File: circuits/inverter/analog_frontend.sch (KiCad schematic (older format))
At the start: 102 parts

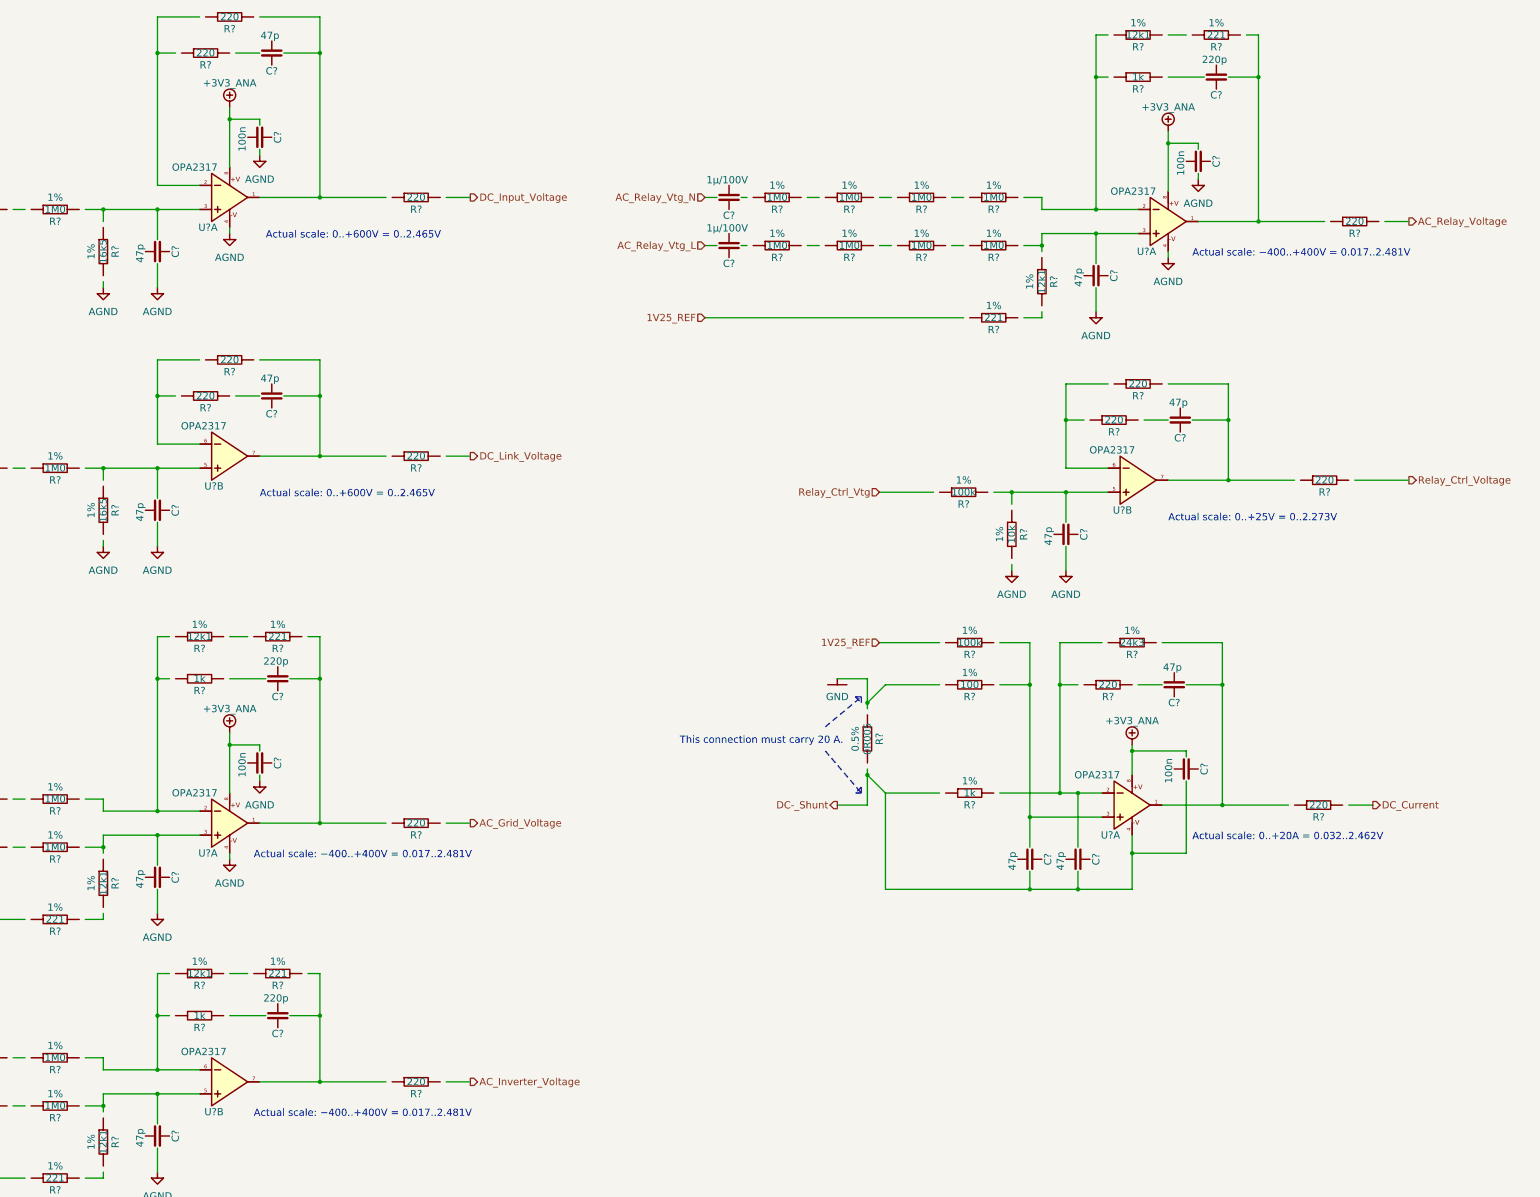
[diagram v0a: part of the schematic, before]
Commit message: Add more circuitry, add library content
AC current measurement
AC filter
AC switch
DC booster
DC input
Analog frontend
drivers
inverter
main controller
power supply

new components for:
standard library (e.g. relay)
AC current sensor acs722
voltage regulator LM317L

Footprints for:
AC relay
TO-220
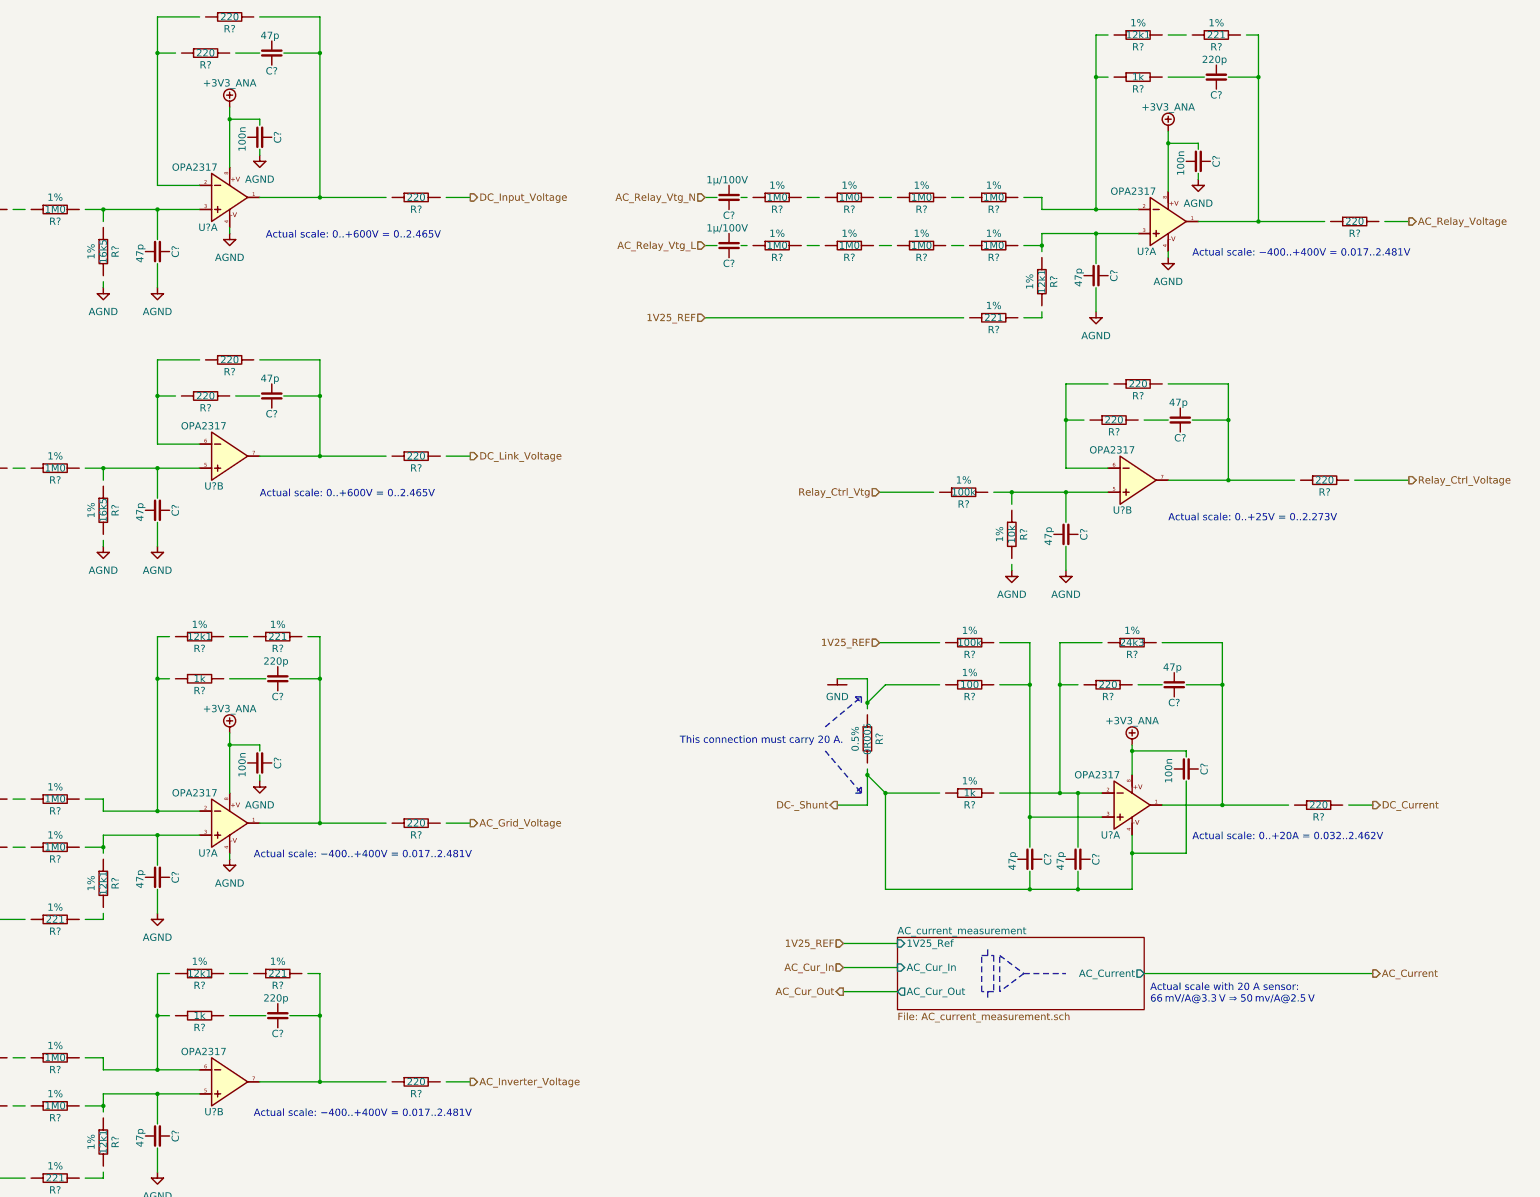
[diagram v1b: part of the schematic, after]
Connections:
- net labels added: AC_Cur_In, AC_Cur_Out, AC_Current
- wire segments 196 -> 249
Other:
- note added: "Actual scale with 20 A sensor:\n66 mV/A@3.3 V ⇒ 50 mv/A@2.5 V"
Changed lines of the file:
@@
 EESchema Schematic File Version 2
+LIBS:lm317
 LIBS:kv30f
 LIBS:OSSI_standard_components
@@
 LIBS:lm4030
 LIBS:power
+LIBS:acs722
 LIBS:OSSI_MK_I-cache
 EELAYER 25 0
@@
 $Descr A3 16535 11693
 encoding utf-8
-Sheet 8 10
+Sheet 8 11
 Title "Analog Frontend"
 Date "2016-03-09"
@@
 	4200 2850 4200 2800
 Wire Wire Line
-	4050 2200 5000 2200
+	4050 2200 4200 2200
+Wire Wire Line
+	4200 2200 4650 2200
+Wire Wire Line
+	4650 2200 5000 2200
 Wire Wire Line
 	4200 2300 4200 2200
@@
 $EndComp
 Wire Wire Line
-	5250 1350 5250 1850
+	5250 1350 5250 1450
+Wire Wire Line
+	5250 1450 5250 1850
 $Comp
 L Capacitor C?
@@
 Connection ~ 5250 1450
 Wire Wire Line
-	5500 2100 6550 2100
+	5500 2100 6000 2100
+Wire Wire Line
+	6000 2100 6550 2100
 $Comp
 L Capacitor C?
@@
 	4650 2000 5000 2000
 Wire Wire Line
-	4650 600  4650 2000
+	4650 600  4650 900
+Wire Wire Line
+	4650 900  4650 2000
 Wire Wire Line
 	4650 600  5000 600
@@
 	5500 600  6000 600
 Wire Wire Line
-	6000 600  6000 2100
+	6000 600  6000 900
+Wire Wire Line
+	6000 900  6000 2100
 Connection ~ 6000 2100
 Wire Wire Line
@@
 	4200 5000 4200 4950
 Wire Wire Line
-	4050 4350 5000 4350
+	4050 4350 4200 4350
+Wire Wire Line
+	4200 4350 4650 4350
+Wire Wire Line
+	4650 4350 5000 4350
 Wire Wire Line
 	4200 4450 4200 4350
@@
 	1400 4350 1750 4350
 Wire Wire Line
-	5500 4250 6550 4250
+	5500 4250 6000 4250
+Wire Wire Line
+	6000 4250 6550 4250
 $Comp
 L Capacitor C?
@@
 	4650 4150 5000 4150
 Wire Wire Line
-	4650 3450 4650 4150
+	4650 3450 4650 3750
+Wire Wire Line
+	4650 3750 4650 4150
 Wire Wire Line
 	4650 3450 5000 3450
@@
 	5500 3450 6000 3450
 Wire Wire Line
-	6000 3450 6000 4250
+	6000 3450 6000 3750
+Wire Wire Line
+	6000 3750 6000 4250
 Connection ~ 6000 4250
 Wire Wire Line
@@
 	4200 8050 4200 8100
 Wire Wire Line
-	4200 7400 5000 7400
-Wire Wire Line
-	4200 7400 4200 7550
+	4200 7400 4650 7400
+Wire Wire Line
+	4650 7400 5000 7400
+Wire Wire Line
+	4200 7400 4200 7500
+Wire Wire Line
+	4200 7500 4200 7550
 Wire Wire Line
 	3550 7500 3450 7500
@@
 $EndComp
 Wire Wire Line
-	5250 6550 5250 7050
+	5250 6550 5250 6650
+Wire Wire Line
+	5250 6650 5250 7050
 $Comp
 L Capacitor C?
@@
 Connection ~ 5250 6650
 Wire Wire Line
-	5500 7300 6550 7300
+	5500 7300 6000 7300
+Wire Wire Line
+	6000 7300 6550 7300
 $Comp
 L Capacitor C?
@@
 $EndComp
 Wire Wire Line
-	4200 7200 5000 7200
+	4200 7200 4650 7200
+Wire Wire Line
+	4650 7200 5000 7200
 Connection ~ 6000 7300
 Wire Wire Line
@@
 	11750 5200 11750 5150
 Wire Wire Line
-	11600 4550 12550 4550
+	11600 4550 11750 4550
+Wire Wire Line
+	11750 4550 12200 4550
+Wire Wire Line
+	12200 4550 12550 4550
 Wire Wire Line
 	11750 4650 11750 4550
@@
 	10650 4550 11100 4550
 Wire Wire Line
-	13050 4450 14100 4450
+	13050 4450 13550 4450
+Wire Wire Line
+	13550 4450 14100 4450
 $Comp
 L Capacitor C?
@@
 	12200 4350 12550 4350
 Wire Wire Line
-	12200 3650 12200 4350
+	12200 3650 12200 3950
+Wire Wire Line
+	12200 3950 12200 4350
 Wire Wire Line
 	12200 3650 12550 3650
@@
 	13050 3650 13550 3650
 Wire Wire Line
-	13550 3650 13550 4450
+	13550 3650 13550 3950
+Wire Wire Line
+	13550 3950 13550 4450
 Connection ~ 13550 4450
 Wire Wire Line
@@
 	4200 7100 4200 7200
 Wire Wire Line
-	4200 9550 5000 9550
-Wire Wire Line
-	5500 9450 6550 9450
+	4200 9550 4650 9550
+Wire Wire Line
+	4650 9550 5000 9550
+Wire Wire Line
+	5500 9450 6000 9450
+Wire Wire Line
+	6000 9450 6550 9450
 $Comp
 L Capacitor C?
@@
 $EndComp
 Wire Wire Line
-	4200 9350 5000 9350
-Wire Wire Line
-	4650 8550 4650 9350
+	4200 9350 4650 9350
+Wire Wire Line
+	4650 9350 5000 9350
+Wire Wire Line
+	4650 8550 4650 8900
+Wire Wire Line
+	4650 8900 4650 9350
 Wire Wire Line
 	4650 8550 4750 8550
 Wire Wire Line
-	6000 8550 6000 9450
+	6000 8550 6000 8900
+Wire Wire Line
+	6000 8900 6000 9450
 Connection ~ 6000 9450
 Wire Wire Line
@@
 	4200 10200 4200 10250
 Wire Wire Line
-	4200 9550 4200 9700
+	4200 9550 4200 9650
+Wire Wire Line
+	4200 9650 4200 9700
 Wire Wire Line
 	3550 9650 3450 9650
@@
 	5900 8550 6000 8550
 Wire Wire Line
-	6000 5750 6000 7300
-Wire Wire Line
-	4650 5750 4650 7200
+	6000 5750 6000 6100
+Wire Wire Line
+	6000 6100 6000 7300
+Wire Wire Line
+	4650 5750 4650 6100
+Wire Wire Line
+	4650 6100 4650 7200
 $Comp
 L Resistor R?
@@
 	12000 3050 12000 3100
 Wire Wire Line
-	12000 2400 12800 2400
-Wire Wire Line
-	12000 2400 12000 2550
+	12000 2400 12450 2400
+Wire Wire Line
+	12450 2400 12800 2400
+Wire Wire Line
+	12000 2400 12000 2500
+Wire Wire Line
+	12000 2500 12000 2550
 Wire Wire Line
 	11350 2500 11250 2500
@@
 $EndComp
 Wire Wire Line
-	13050 1550 13050 2050
+	13050 1550 13050 1650
+Wire Wire Line
+	13050 1650 13050 2050
 $Comp
 L Capacitor C?
@@
 Connection ~ 13050 1650
 Wire Wire Line
-	13300 2300 14350 2300
+	13300 2300 13800 2300
+Wire Wire Line
+	13800 2300 14350 2300
 $Comp
 L Capacitor C?
@@
 $EndComp
 Wire Wire Line
-	12000 2200 12800 2200
+	12000 2200 12450 2200
+Wire Wire Line
+	12450 2200 12800 2200
 Connection ~ 13800 2300
 Wire Wire Line
@@
 $EndComp
 Wire Wire Line
-	13800 750  13800 2300
-Wire Wire Line
-	12450 750  12450 2200
+	13800 750  13800 1100
+Wire Wire Line
+	13800 1100 13800 2300
+Wire Wire Line
+	12450 750  12450 1100
+Wire Wire Line
+	12450 1100 12450 2200
 $Comp
 L Resistor R?
@@
 DC_Current
 Wire Wire Line
-	12750 7850 12750 7400
+	12750 7850 12750 7550
+Wire Wire Line
+	12750 7550 12750 7400
 $Comp
 L +3V3_ANA #+3V3_ANA?
@@
 $EndComp
 Wire Wire Line
-	12750 6650 12750 6900
+	12750 6650 12750 6700
+Wire Wire Line
+	12750 6700 12750 6900
 $Comp
 L Capacitor C?
@@
 Connection ~ 12750 6700
 Wire Wire Line
-	13000 7150 14050 7150
+	13000 7150 13500 7150
+Wire Wire Line
+	13500 7150 14050 7150
 $Comp
 L Capacitor C?
@@
 $EndComp
 Wire Wire Line
-	11650 7050 12500 7050
-Wire Wire Line
-	12150 5800 12150 7050
+	11650 7050 12150 7050
+Wire Wire Line
+	12150 7050 12300 7050
+Wire Wire Line
+	12300 7050 12500 7050
+Wire Wire Line
+	12150 5800 12150 6150
+Wire Wire Line
+	12150 6150 12150 7050
 Wire Wire Line
 	12150 5800 12500 5800
@@
 	13000 5800 13500 5800
 Wire Wire Line
-	13500 5800 13500 7150
+	13500 5800 13500 6150
+Wire Wire Line
+	13500 6150 13500 7150
 Connection ~ 13500 7150
 Wire Wire Line
@@
 	10300 6100 10550 6100
 Wire Wire Line
-	10550 6100 10550 6350
-Wire Wire Line
-	10550 6850 10550 7150
+	10550 6100 10550 6300
+Wire Wire Line
+	10550 6300 10550 6350
+Wire Wire Line
+	10550 6850 10550 6900
+Wire Wire Line
+	10550 6900 10550 7150
 Wire Wire Line
 	10550 7150 10300 7150
@@
 	10700 7050 10700 7850
 Wire Wire Line
-	10700 7850 12750 7850
+	10700 7850 11900 7850
+Wire Wire Line
+	11900 7850 12300 7850
+Wire Wire Line
+	12300 7850 12750 7850
 Wire Wire Line
 	13200 7550 12750 7550
@@
 Connection ~ 11900 7850
 Wire Wire Line
-	11900 5800 11900 7500
+	11900 5800 11900 6150
+Wire Wire Line
+	11900 6150 11900 7250
+Wire Wire Line
+	11900 7250 11900 7500
 Connection ~ 11900 7250
 Wire Wire Line
@@
 	12300 7500 12300 7050
 Connection ~ 12300 7050
+Text HLabel 10350 8500 0    60   Input ~ 0
+AC_Cur_In
+Text HLabel 10350 8700 0    60   Output ~ 0
+AC_Cur_Out
+Text HLabel 14750 8550 2    60   Output ~ 0
+AC_Current
+$Sheet
+S 10800 8250 2050 600
+U 56E3F85C
+F0 "AC_current_measurement" 60
+F1 "AC_current_measurement.sch" 60
+F2 "AC_Cur_In" I L 10800 8500 60
+F3 "AC_Cur_Out" O L 10800 8700 60
+F4 "AC_Current" O R 12850 8550 60
+F5 "1V25_Ref" I L 10800 8300 60
+$EndSheet
+Wire Notes Line
+	11550 8350 11550 8400
+Wire Notes Line
+	11500 8400 11600 8400
+Wire Notes Line
+	11600 8400 11600 8700
+Wire Notes Line
+	11600 8700 11500 8700
+Wire Notes Line
+	11500 8700 11500 8400
+Wire Notes Line
+	11550 8700 11550 8750
+Wire Notes Line
+	11650 8400 11850 8550
+Wire Notes Line
+	11850 8550 11650 8700
+Wire Notes Line
+	11650 8700 11650 8400
+Wire Notes Line
+	11850 8550 12200 8550
+Wire Wire Line
+	12850 8550 14750 8550
+Text HLabel 10350 8300 0    60   Input ~ 0
+1V25_REF
+Wire Wire Line
+	10350 8300 10800 8300
+Wire Wire Line
+	10350 8500 10800 8500
+Wire Wire Line
+	10350 8700 10800 8700
+Text Notes 12900 8800 0    60   ~ 0
+Actual scale with 20 A sensor:\n66 mV/A@3.3 V ⇒ 50 mv/A@2.5 V
+Connection ~ 10700 7050
 $EndSCHEMATC

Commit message: Updates all schematic pages to current components
all components are replaced with the current component library parts
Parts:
- removed C? (x4): 100n, symbol Capacitor
- removed C? (x12): 47p, symbol Capacitor
- removed C? (x3): 220p, symbol Capacitor
- removed C? (x6): 1µ/100V, symbol Capacitor
- removed R? (x32): 1M0, symbol Resistor
- removed R? (x2): 16k5, symbol Resistor
- removed R? (x14): 220, symbol Resistor
- removed R? (x4): 1k, symbol Resistor
- removed R? (x6): 12k1, symbol Resistor
- removed R? (x6): 221, symbol Resistor
- removed R? (x2): 100k, symbol Resistor
- removed R?: 10k, symbol Resistor
- removed R?: 24k3, symbol Resistor
- removed R?: 100, symbol Resistor
- removed U? (x7): OPA2317, symbol DUAL_OPAMP
- added C? (x12): 47p, symbol Capacitor
- added C? (x4): 100n, symbol Capacitor
- added C? (x3): 220p, symbol Capacitor
- added C? (x6): 1µ/100V, symbol Capacitor
- added R? (x32): 1M0, symbol Resistor
- added R? (x2): 16k5, symbol Resistor
- added R? (x14): 220, symbol Resistor
- added R? (x6): 12k1, symbol Resistor
- added R? (x6): 221, symbol Resistor
- added R? (x4): 1k, symbol Resistor
- added R?: 10k, symbol Resistor
- added R? (x3): 100k, symbol Resistor
- added R?: 100, symbol Resistor
- added R?: 24k3, symbol Resistor
- added U? (x8): OPA2317, symbol DUAL_OPAMP
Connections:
- wire segments 249 -> 207
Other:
- note added: "Actual scale with 20 A sensor:\n66 mV/A@3.3 V ⇒ 50 mV/A@2.5 V"
- note removed: "Actual scale with 20 A sensor:\n66 mV/A@3.3 V ⇒ 50 mv/A@2.5 V"
